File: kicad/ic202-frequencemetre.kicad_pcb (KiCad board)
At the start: 2 copper layers, 80 x 50 mm, 49 parts, among them J1 +12V IN (4 pins: 2x+12V, 2x G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, J2 RF IN, J4 LCD, Q1 2SC5551AE-TD-E, U1 AMS1117-5.0, U2 AMS1117 (ADJ), U3 MB506

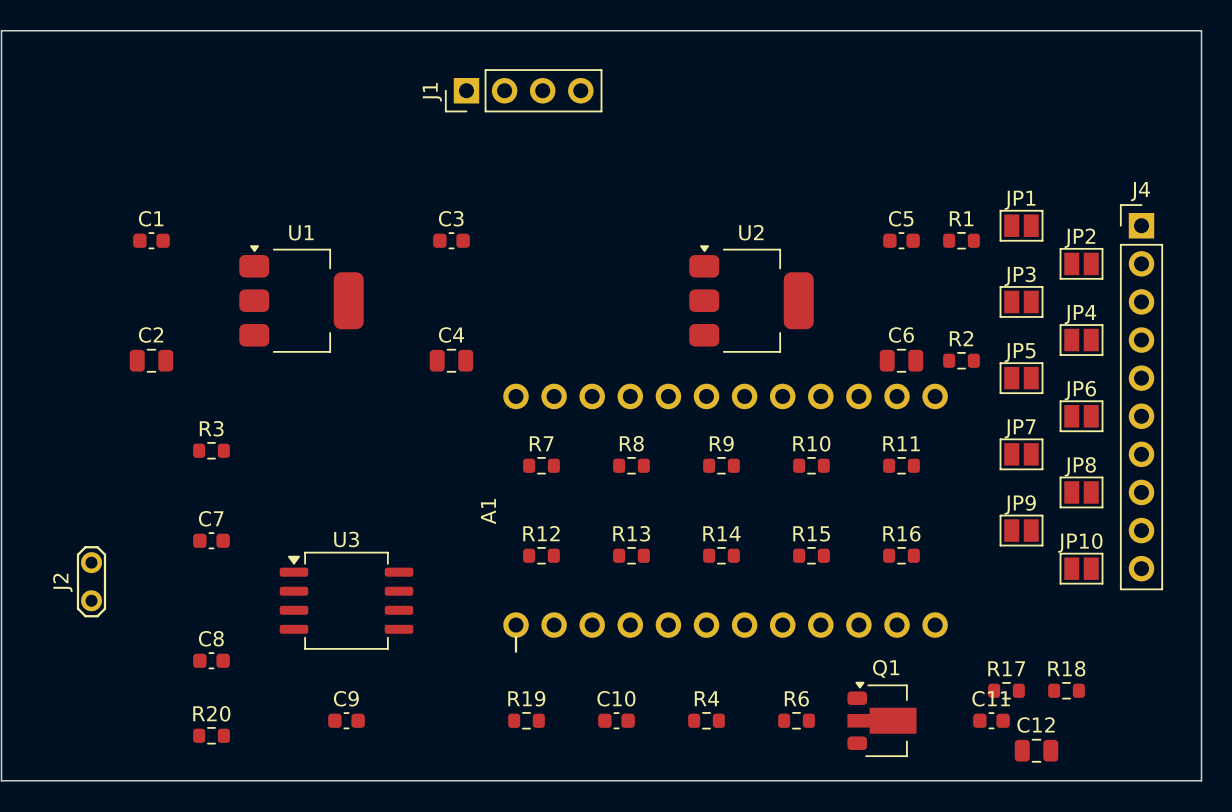
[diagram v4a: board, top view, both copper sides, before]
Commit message: Premier routage complet : 0 erreur DRC
Autoroutage Freerouting (2 couches) sur le placement manuel : 16,5s,
278 pistes + 29 vias. 11 pistes exportees a 0,15mm par le pipeline
KiCad->DSN->Freerouting (la carte impose 0,2mm min, limitation connue et
reproductible du pipeline) corrigees une par une (piste supprimee puis
retracee a 0,2mm au meme endroit).

Comparaison de placement tentee avec l'outil externe FD-Autoplacer
(optimisation par descente de gradient) : resultat non retenu
(chevauchement de courtyard reel, composants debordant du bord de carte).
Le placement manuel a ete conserve ; fichier d'experimentation exclu du
depot (kicad/fd-autoplacer-experiment/, non commite).

run_drc final : 0 erreur, 10 avertissements cosmetiques (vias non
connectees des deux cotes, chevauchements silkscreen).

Co-Authored-By: Claude Sonnet 5 <noreply@anthropic.com>
Claude-Session: https://claude.ai/code/session_017jkpXZgM5sH1vt8JFfAijf
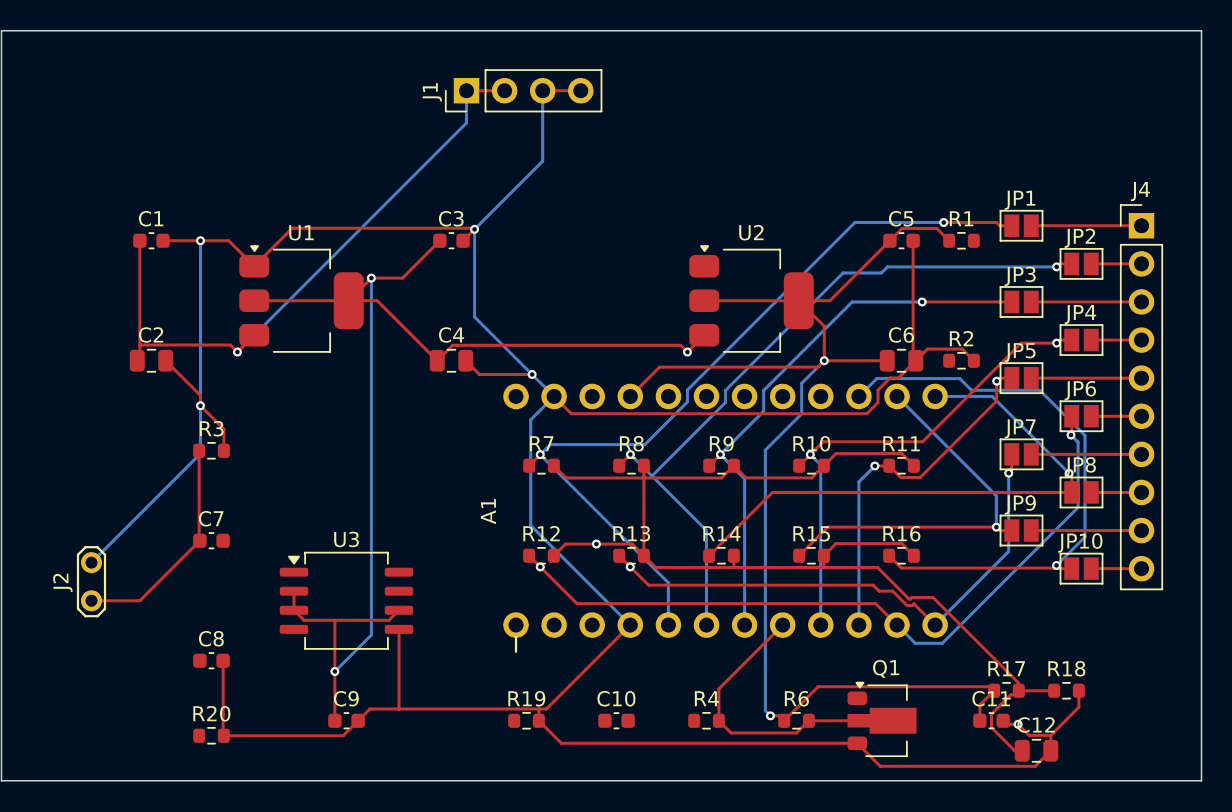
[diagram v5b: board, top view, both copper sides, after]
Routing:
- net GND: track 0.00 -> 230.7 mm, vias 0 -> 5
- net +3V: track 0.00 -> 85.4 mm, vias 0 -> 2
- net VLCD_MID: track 0.00 -> 84.6 mm, vias 0 -> 1
- net +5V: track 0.00 -> 83.2 mm, vias 0 -> 3
- net LCD_COM1: track 0.00 -> 54.3 mm, vias 0 -> 2
- net LCD_SEG2: track 0.00 -> 49.1 mm, vias 0 -> 2
- net LCD_COM2: track 0.00 -> 48.9 mm, vias 0 -> 2
- net +12V: track 0.00 -> 42.6 mm, vias 0 -> 1
- net LCD_SEG6: track 0.00 -> 39.3 mm, vias 0 -> 1
- net LCD_SEG4: track 0.00 -> 38.3 mm, vias 0 -> 1
- net LCD_COM3: track 0.00 -> 37.5 mm, vias 0 -> 2
- net LCD_SEG3: track 0.00 -> 36.6 mm, vias 0 -> 2
- net LCD_COM4: track 0.00 -> 33.3 mm, vias 0 -> 2
- net LCD_SEG5: track 0.00 -> 26.5 mm, vias 0 -> 1
- net LCD_SEG1: track 0.00 -> 24.0 mm, vias 0 -> 2
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
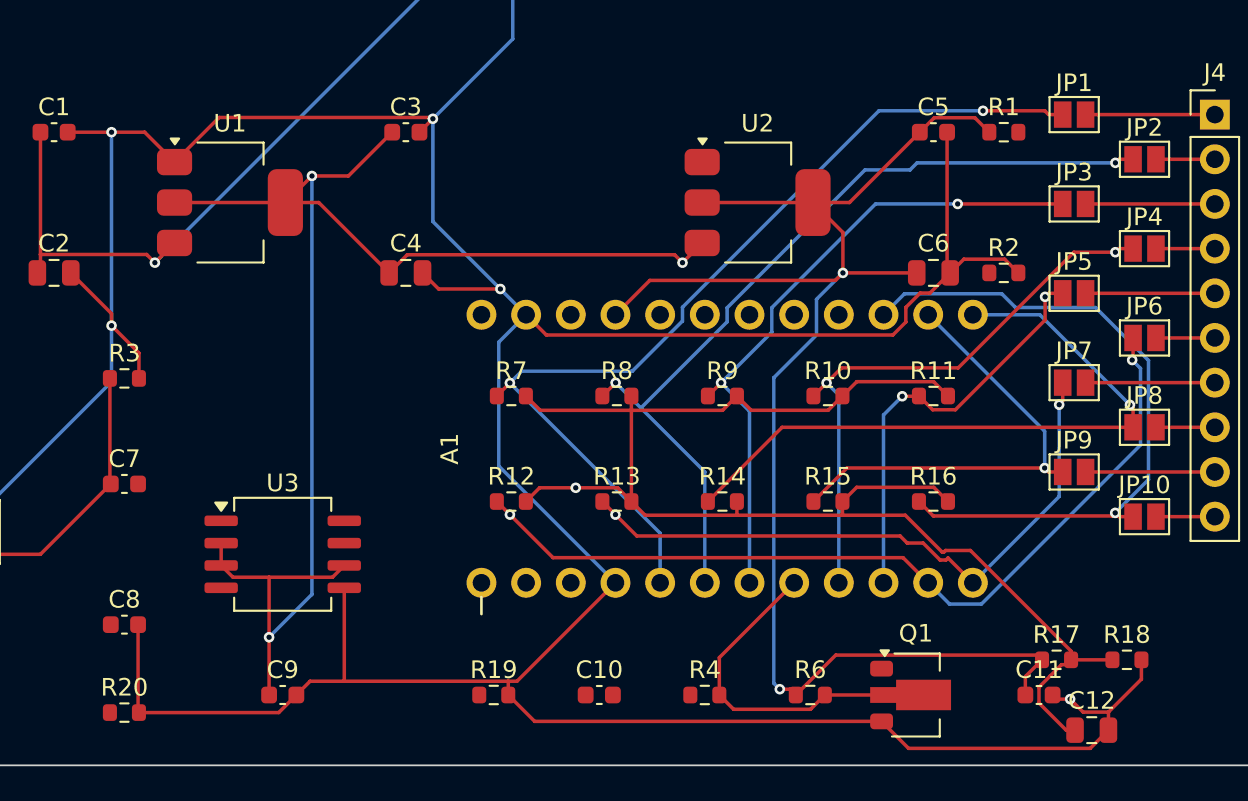
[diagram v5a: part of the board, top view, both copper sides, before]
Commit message: Corrige 5 broches actives sans net (bug critique non detecte par ERC/DRC)
Trouve via inspection visuelle : la broche 1 de U3 semblait connectee a
trop d'endroits. Cause reelle : 5 nets sans label explicite (Net-(U3-IN),
Net-(U3-OUT), Net-(U3-~{IN}), Net-(Q1-B), Net-(U2-ADJ)) - valides au
schema, ERC silencieux - mais que sync_schematic_to_board echoue a
resoudre, laissant ces broches sans net du tout cote PCB. Consequence
reelle : la sortie du prescaler U3 et la base de Q1 n'ont jamais ete
reliees a la chaine de comptage, sur aucune des deux cartes, malgre un DRC
a 0 erreur (une broche sans net n'a aucune obligation de clearance envers
les autres nets).

Corrige :
- 5 nets renommes explicitement (MB506_IN, MB506_OUT, MB506_NIN, Q1_BASE,
  U2_ADJ), verifie via kicad-cli sch export netlist (parse par comptage de
  parentheses) qu'aucun net actif ne reste anonyme.
- Regle de clearance globale du board remontee de 0mm a 0.2mm (masquait
  d'autres risques de contact accidentel sur toute la carte, pas
  seulement a U3).
- Carte principale entierement reroutee (327 pistes, 40 vias) apres
  resynchronisation : 0 erreur run_drc.

Nouvelle regle ajoutee au skill conception-electronique-kicad : verifier
via kicad-cli sch export netlist qu'aucune broche active de composant ne
repose sur un net anonyme (Net-(...)) avant tout premier routage.

Co-Authored-By: Claude Sonnet 5 <noreply@anthropic.com>
Claude-Session: https://claude.ai/code/session_017jkpXZgM5sH1vt8JFfAijf
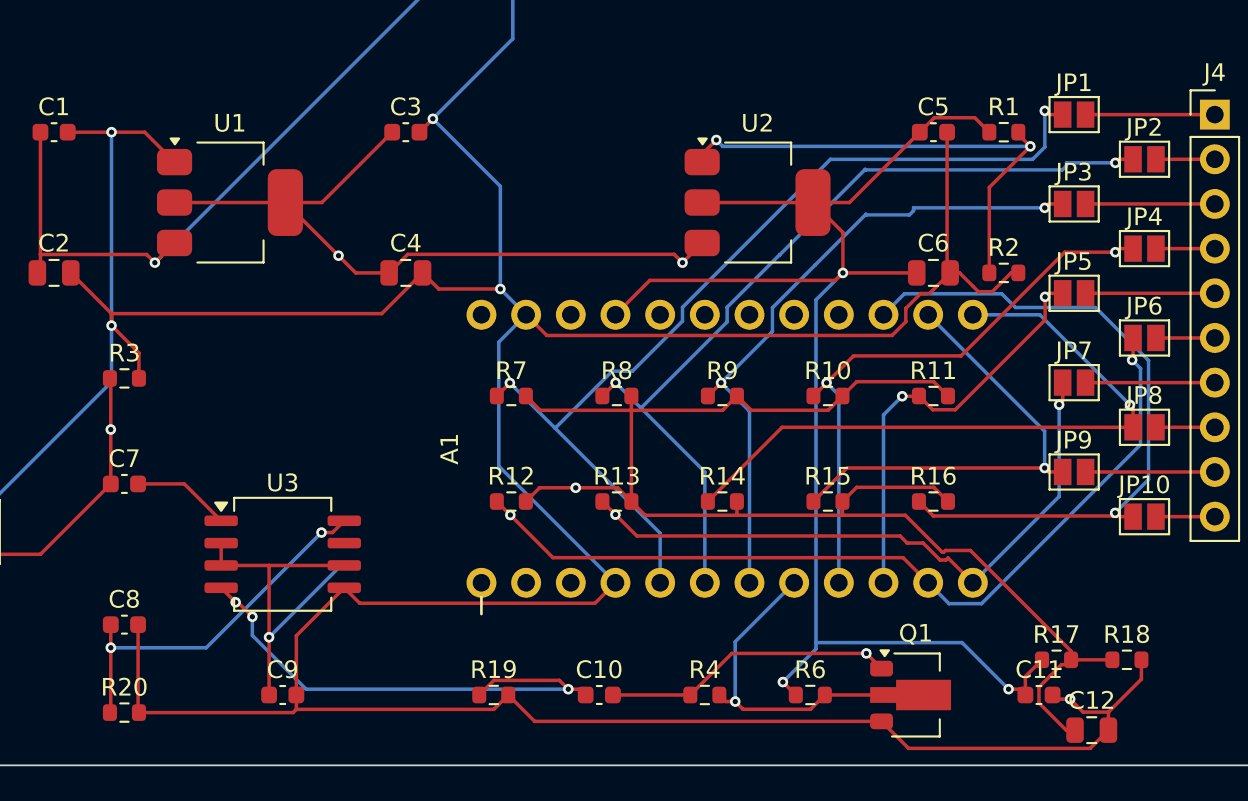
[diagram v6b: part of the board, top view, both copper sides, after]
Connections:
- C10 pad 1: (no net) -> MB506_OUT
- C10 pad 2: (no net) -> Q1_BASE
- C7 pad 2: (no net) -> MB506_IN
- C8 pad 1: (no net) -> MB506_NIN
- Q1 pad 1: (no net) -> Q1_BASE
- R1 pad 2: (no net) -> U2_ADJ
- R19 pad 1: (no net) -> MB506_OUT
- R2 pad 1: (no net) -> U2_ADJ
- R20 pad 1: (no net) -> MB506_NIN
- R4 pad 1: (no net) -> Q1_BASE
- U2 pad 1: (no net) -> U2_ADJ
- U3 pad 1: (no net) -> MB506_IN
- U3 pad 4: (no net) -> MB506_OUT
- U3 pad 8: (no net) -> MB506_NIN
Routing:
- net MB506_OUT: track 0.00 -> 29.5 mm, vias 0 -> 3
- net U2_ADJ: track 0.00 -> 28.8 mm, vias 0 -> 2
- net +5V: track 83.2 -> 61.7 mm
- net MB506_NIN: track 0.00 -> 21.3 mm, vias 0 -> 2
- net Q1_BASE: track 0.00 -> 16.6 mm, vias 0 -> 1
- net GND: track 230.7 -> 243.3 mm
- net MB506_IN: track 0.00 -> 5.59 mm
- net +3V: track 85.4 -> 82.7 mm, vias 2 -> 3
- net D5_SIG: vias 0 -> 1
- net RF_IN: vias 0 -> 1

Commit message: Corrige fp-lib-table fd-placed et reroute; ajoute doc LCD
- kicad/fd-autoplacer-experiment/fp-lib-table (nouveau) : enregistre la
  bibliotheque locale "frequencemetre" pour ce sous-projet (jusqu'ici
  invisible faute de fp-lib-table propre a ce dossier -> warning DRC
  "does not include the footprint library 'frequencemetre'").
- fd-placed : reload + effacement + reautoroutage complet (32/32 nets)
  apres application de la correction ci-dessus ; verifie via
  find_wrong_face_stubs.py (0 piste mal orientee). Les etiquettes de face
  incoherentes (lib_footprint_mismatch, 22 cas) etaient deja resolues par
  une sauvegarde depuis l'editeur KiCad entre-temps.
- kicad/frequencemetre.pretty/Arduino_Pro_Mini_Header_2x12.kicad_mod :
  resauvegarde par KiCad 10 (generator_version 9.0 -> 10.0), pas de
  changement fonctionnel (24 pastilles inchangees).
- Reste 1 erreur DRC connue sur fd-placed : chevauchement de courtyard
  C8/R20 (composants places quasi au meme point) - a regler cote
  placement, hors perimetre de ce commit.
- kicad/ic202-frequencemetre.kicad_pcb/.kicad_pro : etat courant de la
  carte principale.
- docs/LCD_2.png : ajout documentation.

Co-Authored-By: Claude Sonnet 5 <noreply@anthropic.com>
Claude-Session: https://claude.ai/code/session_017jkpXZgM5sH1vt8JFfAijf
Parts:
- moved A1 73.4 mm to (111.5, 67.0)
- moved C1 73.4 mm to (74.5, 49.0)
- moved C10 73.4 mm to (105.5, 81.0)
- moved C11 73.4 mm to (130.5, 81.0)
- moved C12 73.4 mm to (133.5, 83.0)
- moved C2 73.4 mm to (74.5, 57.0)
- moved C3 73.4 mm to (94.5, 49.0)
- moved C4 73.4 mm to (94.5, 57.0)
- moved C5 73.4 mm to (124.5, 49.0)
- moved C6 73.4 mm to (124.5, 57.0)
- moved C7 73.4 mm to (78.5, 69.0)
- moved C8 73.4 mm to (78.5, 77.0)
- moved C9 73.4 mm to (87.5, 81.0)
- moved J1 73.4 mm to (95.5, 39.0)
- moved J2 73.4 mm to (70.5, 73.0)
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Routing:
- net +5V: track 61.7 -> 56.1 mm, vias 3 -> 0
- net LCD_SEG3: track 36.6 -> 37.0 mm, vias 2 -> 1
- net LCD_COM4: track 33.3 -> 33.4 mm, vias 2 -> 1
- net GND: vias 5 -> 4
- net VLCD_MID: vias 1 -> 0
- net LCD_SEG2: vias 2 -> 1
- net RF_IN: vias 1 -> 0
- net Q1_BASE: vias 1 -> 0
- net LCD_SEG1: vias 2 -> 1
- net MB506_OUT: vias 3 -> 2
